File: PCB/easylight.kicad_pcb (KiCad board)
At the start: 2 copper layers, 50.2 x 41.3 mm, 49 parts, among them J1 LiPo (1S/3.7V), J2 USB/PWR, J3 LEDs, J4 AVR-ISP, J8 SW4+, Q1 AO3415_C181094, Q2 AO3415_C181094, SW0 SPEF110100, SW1 TS-1187A-B-A-B, SW2 TS-1187A-B-A-B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

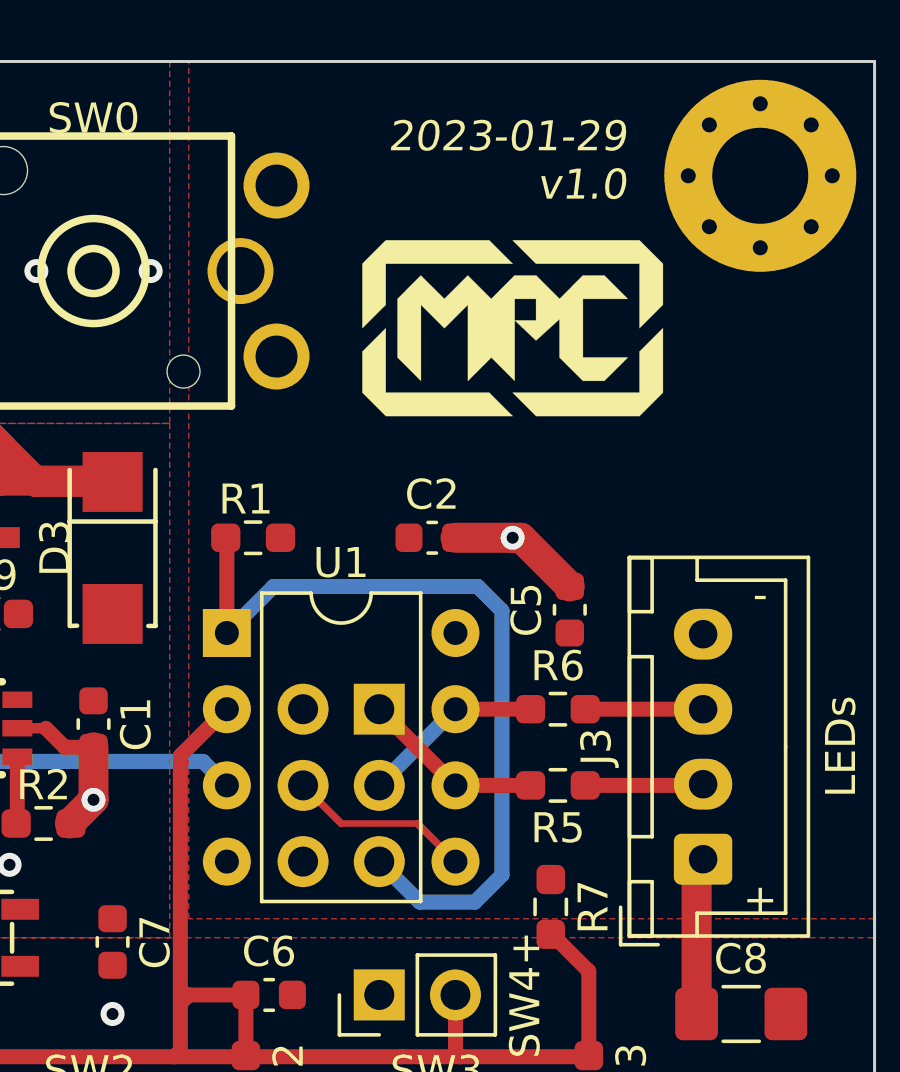
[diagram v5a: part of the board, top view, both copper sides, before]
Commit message: use specific isp connector that has polarity marker, update revision to v1.1, set board colors
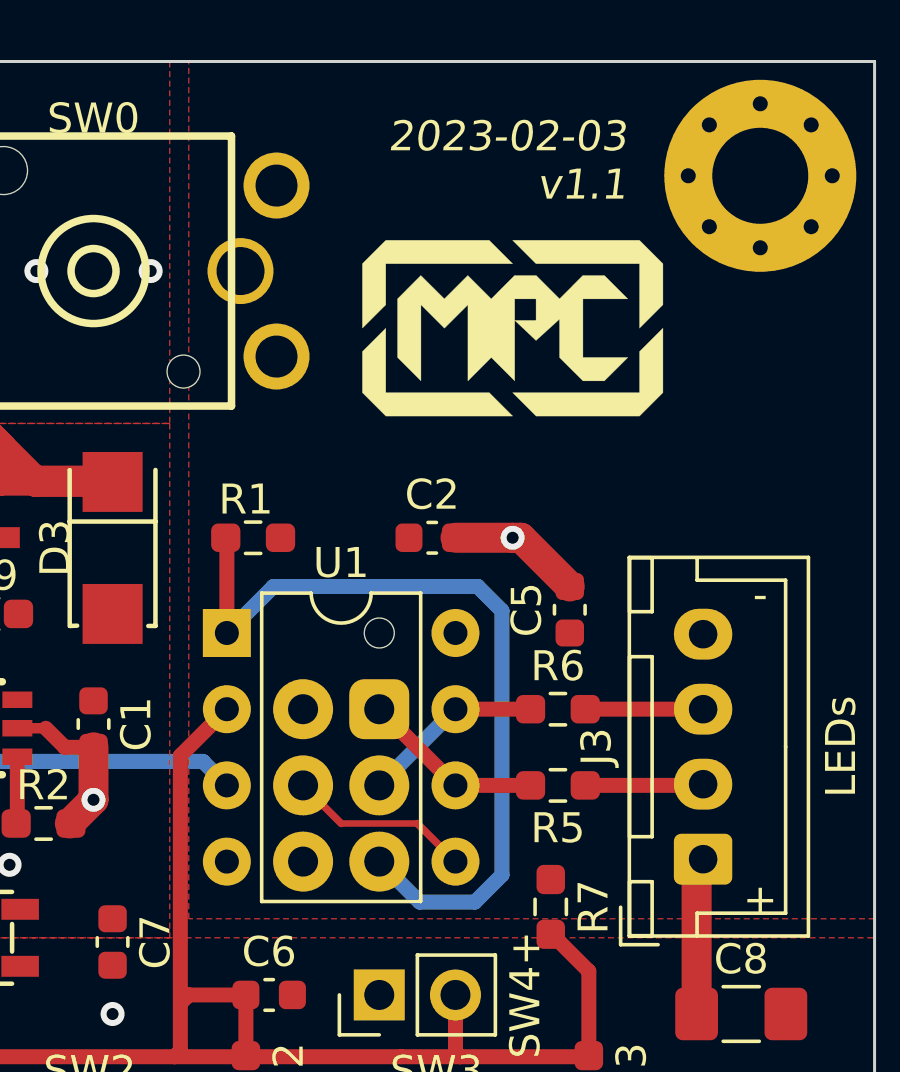
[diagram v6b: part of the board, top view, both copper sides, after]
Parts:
- J4: footprint Connector_PinHeader_2.54mm:PinHeader_2x03_P2.54mm_Vertical -> ModischFabrications:3x2 CopperPad 2.54mm
- moved J4 2.84 mm to (70.5, 66.0)
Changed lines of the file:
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@@
   (title_block
     (title "EasyLight")
-    (date "2023-01-29")
-    (rev "1.0")
+    (date "2023-02-03")
+    (rev "1.1")
     (company "MPC")
   )
@@
   )
   (setup
+    (stackup
+      (layer "F.SilkS" (type "Top Silk Screen") (color "White"))
+      (layer "F.Paste" (type "Top Solder Paste"))
+      (layer "F.Mask" (type "Top Solder Mask") (color "Blue") (thickness 0.01))
+      (layer "F.Cu" (type "copper") (thickness 0.035))
+      (layer "dielectric 1" (type "core") (thickness 1.51) (material "FR4") (epsilon_r 4.5) (loss_tangent 0.02))
+      (layer "B.Cu" (type "copper") (thickness 0.035))
+      (layer "B.Mask" (type "Bottom Solder Mask") (color "Blue") (thickness 0.01))
+      (layer "B.Paste" (type "Bottom Solder Paste"))
+      (layer "B.SilkS" (type "Bottom Silk Screen") (color "White"))
+      (copper_finish "None")
+      (dielectric_constraints no)
+    )
     (pad_to_mask_clearance 0)
     (pcbplotparams
@@
     )
   )
-  (footprint "Connector_PinHeader_2.54mm:PinHeader_2x03_P2.54mm_Vertical" (layer "B.Cu")
-    (at 71.755 63.5 180)
-    (descr "Through hole straight pin header, 2x03, 2.54mm pitch, double rows")
-    (tags "Through hole pin header THT 2x03 2.54mm double row")
-    (property "Sheetfile" "easylight.kicad_sch")
-    (property "Sheetname" "")
-    (attr through_hole)
-    (fp_text reference "J4" (at 1.27 2.33) (layer "B.Fab")
+  (footprint "ModischFabrications:3x2 CopperPad 2.54mm" (layer "B.Cu")
+    (at 70.485 66.04 180)
+    (property "Sheetfile" "easylight.kicad_sch")
+    (property "Sheetname" "")
+    (fp_text reference "J4" (at 1.27 5.08 unlocked) (layer "B.SilkS")
       (effects (font (size 1 1) (thickness 0.15)) (justify mirror))
     )
-    (fp_text value "AVR-ISP" (at 1.27 -7.41) (layer "B.SilkS")
+    (fp_text value "AVR-ISP" (at 0 -5.08 unlocked) (layer "B.Fab")
       (effects (font (size 1 1) (thickness 0.15)) (justify mirror))
     )
-    (fp_text user "${REFERENCE}" (at 1.27 -2.54 270) (layer "B.Fab")
-      (effects (font (size 1 1) (thickness 0.15)) (justify mirror))
-    )
-    (fp_line (start 1.27 1.33) (end 3.87 1.33) (layer "B.SilkS") (width 0.12))
-    (fp_line (start -1.33 0) (end -1.33 1.33) (layer "B.SilkS") (width 0.12))
-    (fp_line (start -1.33 -1.27) (end -1.33 -6.41) (layer "B.SilkS") (width 0.12))
-    (fp_line (start -1.33 -1.27) (end 1.27 -1.27) (layer "B.SilkS") (width 0.12))
-    (fp_line (start -1.33 -6.41) (end 3.87 -6.41) (layer "B.SilkS") (width 0.12))
-    (fp_line (start -1.33 1.33) (end 0 1.33) (layer "B.SilkS") (width 0.12))
-    (fp_line (start 3.87 1.33) (end 3.87 -6.41) (layer "B.SilkS") (width 0.12))
-    (fp_line (start 1.27 -1.27) (end 1.27 1.33) (layer "B.SilkS") (width 0.12))
-    (fp_line (start -1.8 1.8) (end -1.8 -6.85) (layer "B.CrtYd") (width 0.05))
-    (fp_line (start 4.35 -6.85) (end 4.35 1.8) (layer "B.CrtYd") (width 0.05))
-    (fp_line (start 4.35 1.8) (end -1.8 1.8) (layer "B.CrtYd") (width 0.05))
-    (fp_line (start -1.8 -6.85) (end 4.35 -6.85) (layer "B.CrtYd") (width 0.05))
-    (fp_line (start -1.27 -6.35) (end -1.27 0) (layer "B.Fab") (width 0.1))
-    (fp_line (start 3.81 -6.35) (end -1.27 -6.35) (layer "B.Fab") (width 0.1))
-    (fp_line (start 3.81 1.27) (end 3.81 -6.35) (layer "B.Fab") (width 0.1))
-    (fp_line (start 0 1.27) (end 3.81 1.27) (layer "B.Fab") (width 0.1))
-    (fp_line (start -1.27 0) (end 0 1.27) (layer "B.Fab") (width 0.1))
-    (pad "1" thru_hole rect (at 0 0 180) (size 1.7 1.7) (drill 1) (layers *.Cu *.Mask)
+    (fp_line (start -2.54 3.175) (end -1.905 3.81) (layer "B.CrtYd") (width 0.12))
+    (fp_rect (start -2.54 3.81) (end 2.54 -3.81) (layer "B.CrtYd") (width 0.12) (fill none))
+    (pad "" np_thru_hole circle (at -1.27 5.08 180) (size 1 1) (drill 1) (layers *.Mask))
+    (pad "1" thru_hole roundrect (at -1.27 2.54 180) (size 2 2) (drill 1) (layers *.Cu *.Mask) (roundrect_rratio 0.25)
       (net 4 "/D_LEDS") (pinfunction "MISO") (pintype "passive"))
-    (pad "2" thru_hole oval (at 2.54 0 180) (size 1.7 1.7) (drill 1) (layers *.Cu *.Mask)
+    (pad "2" thru_hole circle (at 1.27 2.54 180) (size 2 2) (drill 1) (layers *.Cu *.Mask)
       (net 1 "VCC") (pinfunction "VCC") (pintype "passive"))
-    (pad "3" thru_hole oval (at 0 -2.54 180) (size 1.7 1.7) (drill 1) (layers *.Cu *.Mask)
+    (pad "3" thru_hole circle (at -1.27 0 180) (size 2 2) (drill 1) (layers *.Cu *.Mask)
       (net 13 "/D_LEDS2") (pinfunction "SCK") (pintype "passive"))
-    (pad "4" thru_hole oval (at 2.54 -2.54 180) (size 1.7 1.7) (drill 1) (layers *.Cu *.Mask)
+    (pad "4" thru_hole circle (at 1.27 0 180) (size 2 2) (drill 1) (layers *.Cu *.Mask)
       (net 16 "/AREF") (pinfunction "MOSI") (pintype "passive"))
-    (pad "5" thru_hole oval (at 0 -5.08 180) (size 1.7 1.7) (drill 1) (layers *.Cu *.Mask)
+    (pad "5" thru_hole circle (at -1.27 -2.54 180) (size 2 2) (drill 1) (layers *.Cu *.Mask)
       (net 15 "/RESET") (pinfunction "~{RST}") (pintype "passive"))
-    (pad "6" thru_hole oval (at 2.54 -5.08 180) (size 1.7 1.7) (drill 1) (layers *.Cu *.Mask)
+    (pad "6" thru_hole circle (at 1.27 -2.54 180) (size 2 2) (drill 1) (layers *.Cu *.Mask)
       (net 2 "GND") (pinfunction "GND") (pintype "passive"))
-    (model "${KICAD6_3DMODEL_DIR}/Connector_PinHeader_2.54mm.3dshapes/PinHeader_2x03_P2.54mm_Vertical.wrl"
-      (offset (xyz 0 0 0))
-      (scale (xyz 1 1 1))
-      (rotate (xyz 0 0 0))
-    )
   )
   (footprint "Symbol:ESD-Logo_6.6x6mm_SilkScreen" (layer "B.Cu")
